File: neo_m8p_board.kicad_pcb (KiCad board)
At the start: 2 copper layers, 42.6 x 38.8 mm, 14 parts, among them J1 SMA, J3 Conn_01x05, J4 Conn_01x06, U1 NEO-M8P

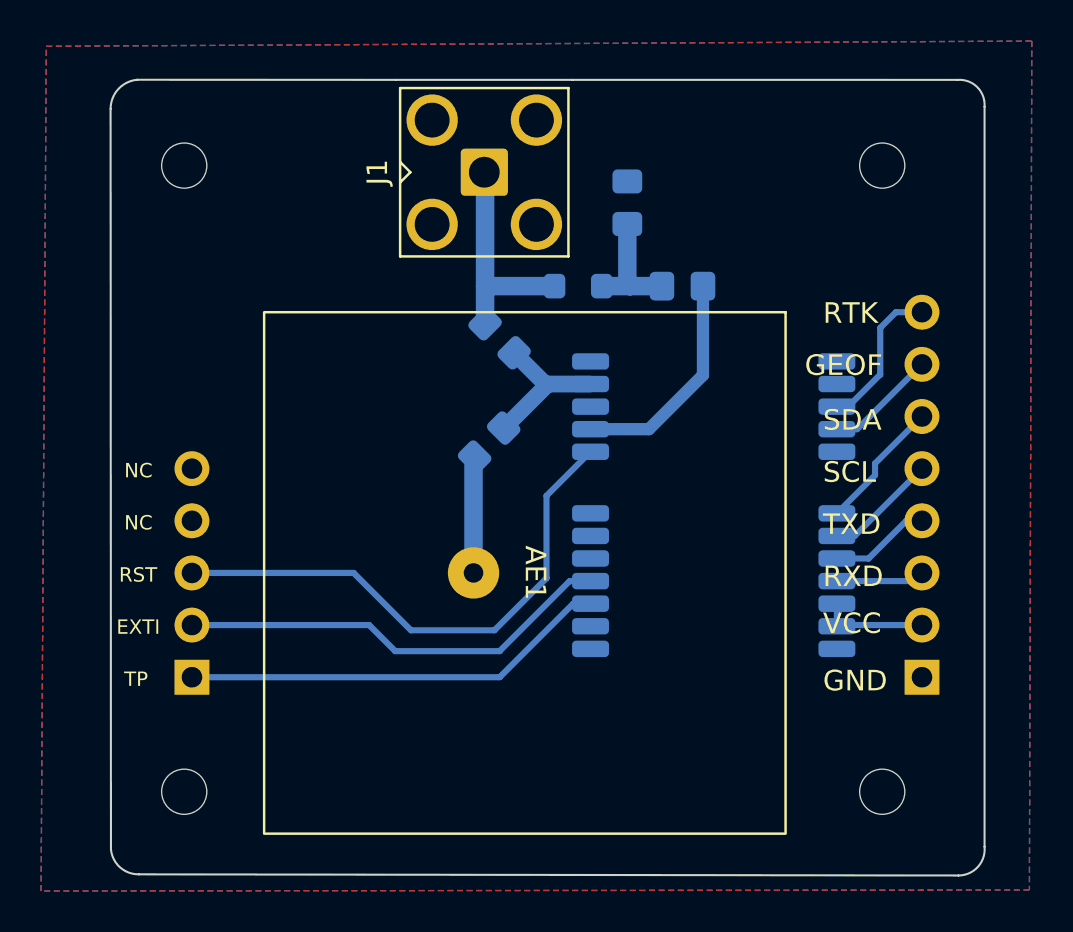
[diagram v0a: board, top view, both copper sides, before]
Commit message: v2: sma antenna only
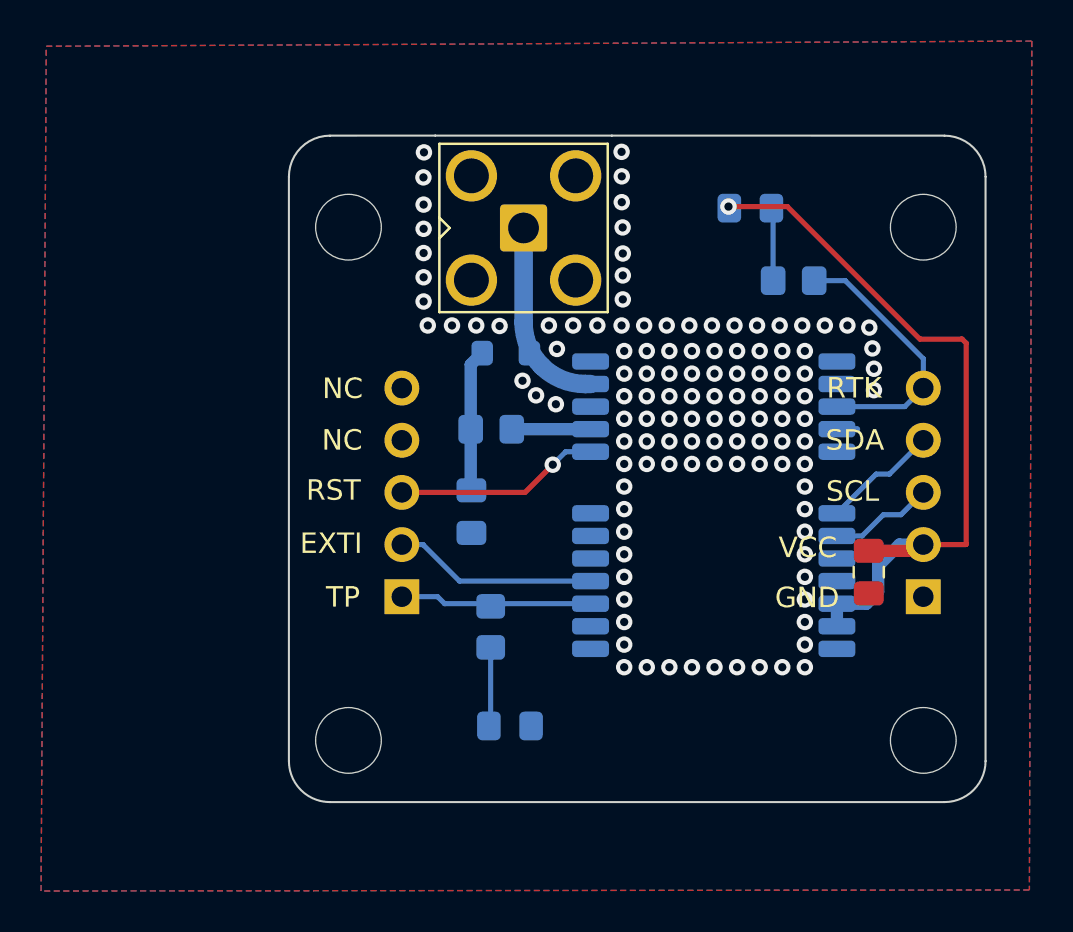
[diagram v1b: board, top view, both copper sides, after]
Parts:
- removed AE1: Antenna, NEO-M8P-Library:GPS_Patch_Antenna_Amphenol
- added C2: 10uF, Capacitor_SMD:C_0805_2012Metric_Pad1.18x1.45mm_HandSolder, F.Cu at (120.3, 132.8)
- added D1: RTK, LED_SMD:LED_0805_2012Metric_Pad1.15x1.40mm_HandSolder, B.Cu at (114.6, 115.1)
- added D2: TP, LED_SMD:LED_0805_2012Metric_Pad1.15x1.40mm_HandSolder, B.Cu at (102.9, 140.3)
- H1, H2, H3, H4: footprint MountingHole:MountingHole_2.2mm_M2 -> MountingHole:MountingHole_3.2mm_M3
- J4: value Conn_01x06 -> Conn_01x05; footprint Connector_PinHeader_2.54mm:PinHeader_1x08_P2.54mm_Vertical -> Connector_PinHeader_2.54mm:PinHeader_1x05_P2.54mm_Vertical
- R2, R3: value 0 -> 1k
- moved C1 16.9 mm to (101.0, 129.9), turned to -90 degrees
- moved R2 16.8 mm to (116.7, 118.6), turned to 180 degrees
- moved R3 14.1 mm to (101.9, 135.5), turned to -90 degrees
- moved R1 11.6 mm to (102.0, 125.8)
- moved J3 11.0 mm to (97.6, 134.0)
- moved H1 8.54 mm to (95.0, 116.0)
- moved H3 8.38 mm to (95.0, 141.0)
- moved L1 4.80 mm to (102.7, 122.1), turned to 0 degrees
- moved J4 3.92 mm to (123.0, 134.0)
- moved H2 3.61 mm to (123.0, 116.0)
- moved J1 3.32 mm to (103.5, 116.0)
- moved H4 3.20 mm to (123.0, 141.0)
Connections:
- net +3.3V renamed +3V3
- J4 pad 3: RXD/SPI_MOSI -> SCL
- J4 pad 4: TXD/SPI_MISO -> SDA
- J4 pad 5: SCL -> RTK_STAT
- R2 pad 1: Net-(AE1-A) -> RTK_STAT
- R2 pad 2: Net-(U1-RF_IN) -> Net-(D1-K)
- R3 pad 1: Net-(U1-RF_IN) -> TIMEPULSE
- R3 pad 2: Net-(J1-In) -> Net-(D2-A)
- U1 pad 11: Net-(U1-RF_IN) -> Net-(J1-In)
- U1 pad 16: GEOFENCE_STAT -> unconnected-(U1-GEOFENCE_STAT-Pad16)
- U1 pad 20: TXD/SPI_MISO -> unconnected-(U1-TXD/SPI_MISO-Pad20)
- U1 pad 21: RXD/SPI_MOSI -> unconnected-(U1-RXD/SPI_MOSI-Pad21)
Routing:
- net +3V3: track 5.27 -> 36.3 mm, vias 0 -> 1
- net RESET_N: track 26.5 -> 10.1 mm, vias 0 -> 1
- net TIMEPULSE: track 20.9 -> 9.33 mm
- net EXTINT: track 21.4 -> 9.93 mm
- net Net-(U1-RF_IN): track 9.47 -> 0.00 mm
- net Net-(U1-VCC_RF): track 10.9 -> 3.84 mm
- net Net-(AE1-A): track 5.67 -> 0.00 mm
- net RTK_STAT: track 7.38 -> 12.9 mm
- net GEOFENCE_STAT: track 5.45 -> 0.00 mm
- net TXD/SPI_MISO: track 4.91 -> 0.00 mm
- net RXD/SPI_MOSI: track 4.31 -> 0.00 mm
- net Net-(D2-A): track 0.00 -> 3.86 mm
- net Net-(D1-K): track 0.00 -> 3.57 mm
- net Net-(J1-In): track 10.9 -> 9.55 mm
- net unconnected-(U1-GEOFENCE_STAT-Pad16): track 0.00 -> 0.99 mm
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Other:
- board size 42.6 x 38.8 mm -> 33.9 x 32.5 mm
- board text removed: "GEOF"
- board text removed: "RESET_N"
- board text removed: "RTK_STAT"
- board text removed: "RXD"
- board text removed: "TXD"
